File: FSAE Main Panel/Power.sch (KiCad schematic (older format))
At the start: 18 parts, among them Q301 Q_PMOS_GSD, U301 LM2734, U302 LP2985-3.3

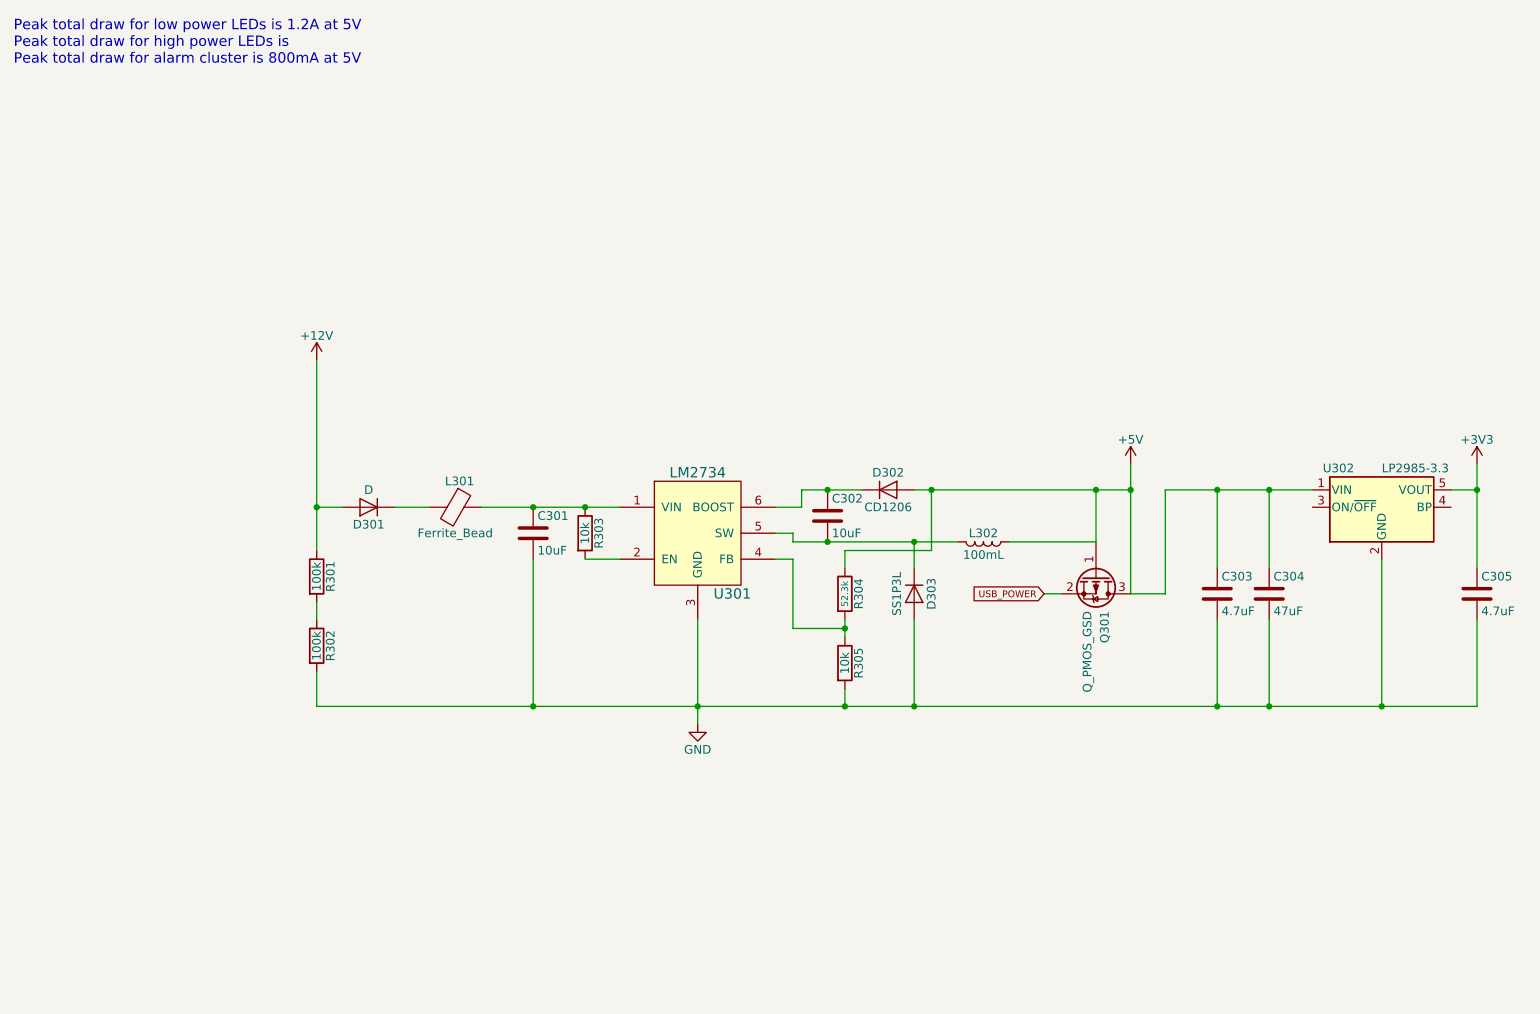
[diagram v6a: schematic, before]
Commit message: Updated power circuit for MCU, used small components on main sheet
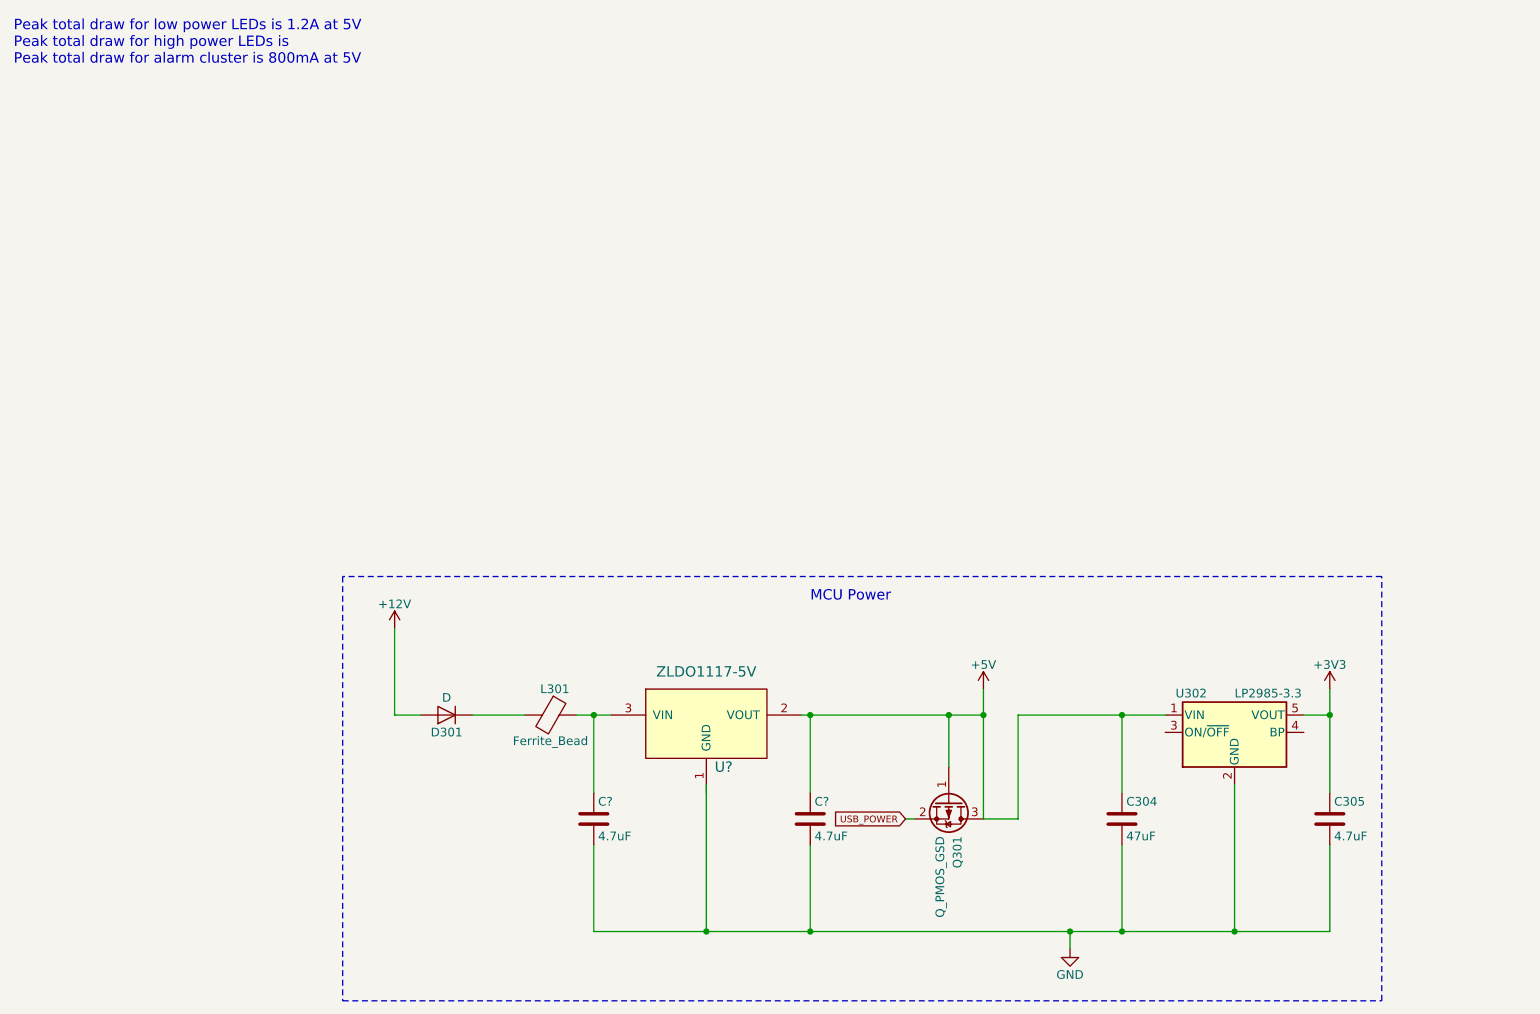
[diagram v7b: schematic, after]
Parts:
- removed C301, C302: 10uF, symbol C
- removed C303: 4.7uF, symbol C
- removed D302: CD1206, symbol D
- removed D303: SS1P3L, symbol D
- removed L302: 100mL, symbol L
- removed R301, R302: 100k, symbol R
- removed R303, R305: 10k, symbol R
- removed R304: 52.3k, symbol R
- removed U301: LM2734, TO_SOT_Packages_SMD:SOT-23-6, symbol LM2734
- added C? (x2): 4.7uF, symbol C
- added U?: ZLDO1117-5V, symbol ZLDO1117-5V
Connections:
- wire segments 63 -> 35
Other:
- note added: "MCU Power"
- moved on the sheet: C304, C305, D301, L301, Q301, U302

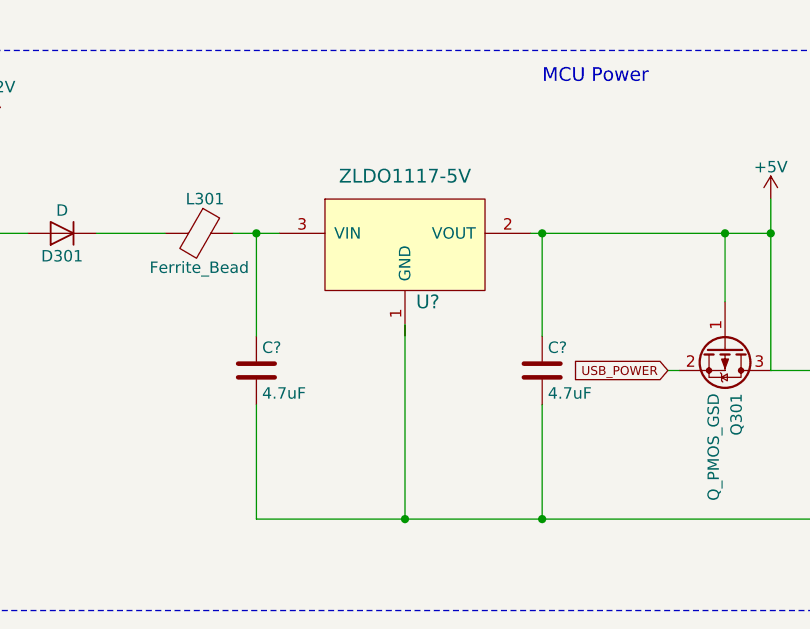
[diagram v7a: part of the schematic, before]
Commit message: Cortex debugger, GPIO pinning, minor fixes
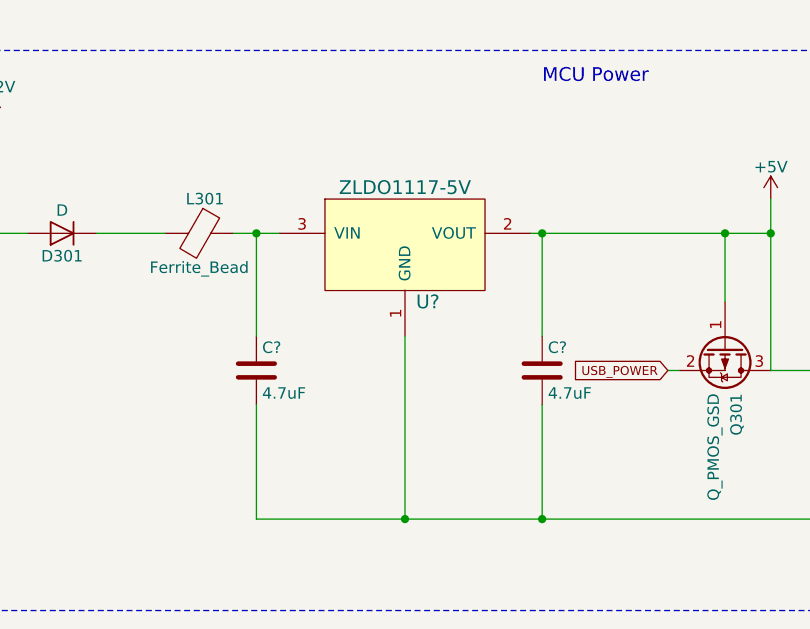
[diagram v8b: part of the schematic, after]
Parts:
- removed U?: ZLDO1117-5V, symbol ZLDO1117-5V
- added U?: ZLDO1117-5V, symbol ZLDO1117-5V
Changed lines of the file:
@@
 LIBS:samd21g18a-au
 LIBS:zldo1117-5v
+LIBS:cortex_debug
 LIBS:FSAE Main Panel-cache
 EELAYER 25 0
@@
 Wire Wire Line
 	6000 4600 6200 4600
-$Comp
-L ZLDO1117-5V U?
-U 1 1 5BF9BBC8
-P 4600 4600
-F 0 "U?" H 4700 4300 60  0000 C CNN
-F 1 "ZLDO1117-5V" H 4600 4850 60  0000 C CNN
-F 2 "" H 4600 4600 60  0001 C CNN
-F 3 "" H 4600 4600 60  0001 C CNN
-	1    4600 4600
-	1    0    0    -1
-$EndComp
-Wire Wire Line
-	4600 5000 4600 5850
+Wire Wire Line
+	4600 5050 4600 5850
 Wire Wire Line
 	6700 5950 6700 5850
@@
 Text Notes 5200 3950 0    60   ~ 0
 MCU Power
+$Comp
+L ZLDO1117-5V U?
+U 1 1 5BFDDF95
+P 4600 4600
+F 0 "U?" H 4700 4300 60  0000 C CNN
+F 1 "ZLDO1117-5V" H 4600 4800 60  0000 C CNN
+F 2 "" H 4600 4600 60  0001 C CNN
+F 3 "" H 4600 4600 60  0001 C CNN
+	1    4600 4600
+	1    0    0    -1
+$EndComp
 $EndSCHEMATC
